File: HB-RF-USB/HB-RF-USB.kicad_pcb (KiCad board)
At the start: 2 copper layers, 47.6 x 52.1 mm, 27 parts, among them J1 USB_B_Micro, J2 Conn_02x20_Odd_Even, J3 Conn_02x06_Odd_Even, Q1 IRLML6402, Q2 IRLML6402, Q3 IRLML2502, U1 FT232RL

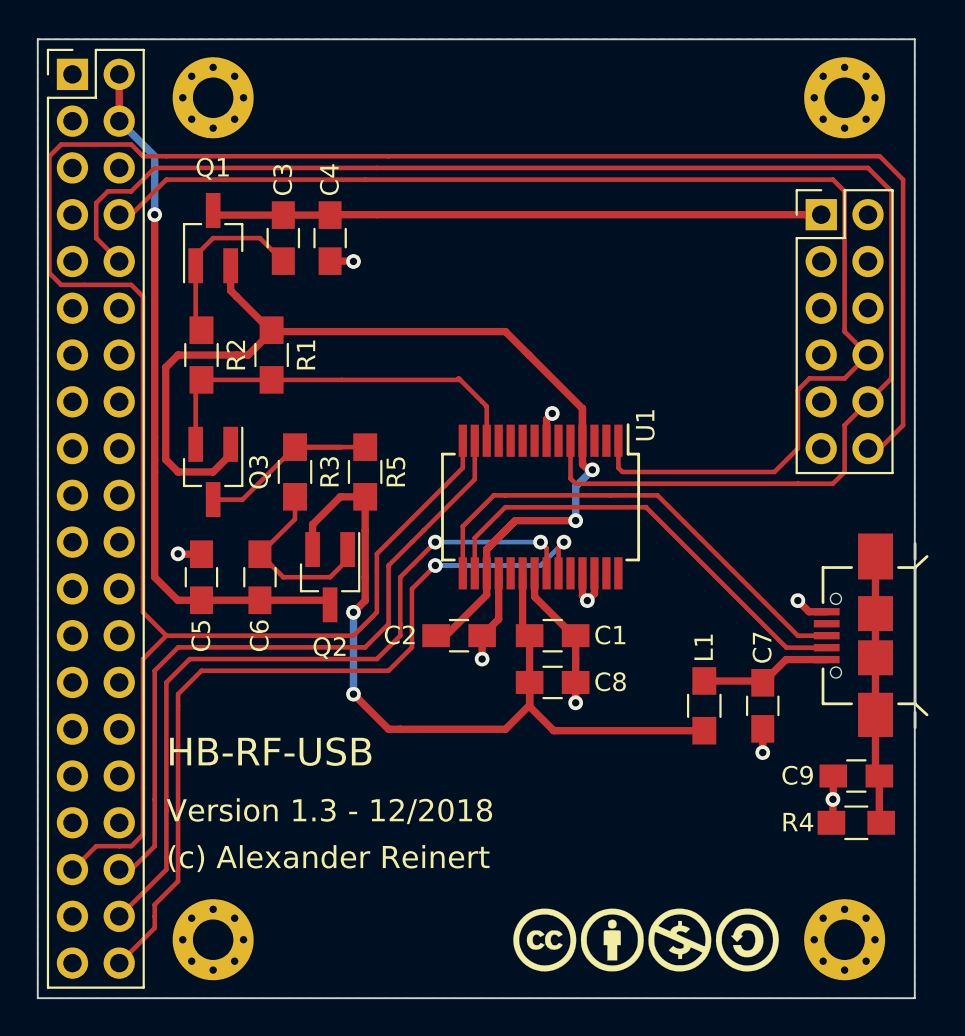
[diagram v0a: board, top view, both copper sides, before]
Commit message: - Update to Kicad 5 symbol and footprint libs
- Use different Micro USB Connector for better mechanical stability
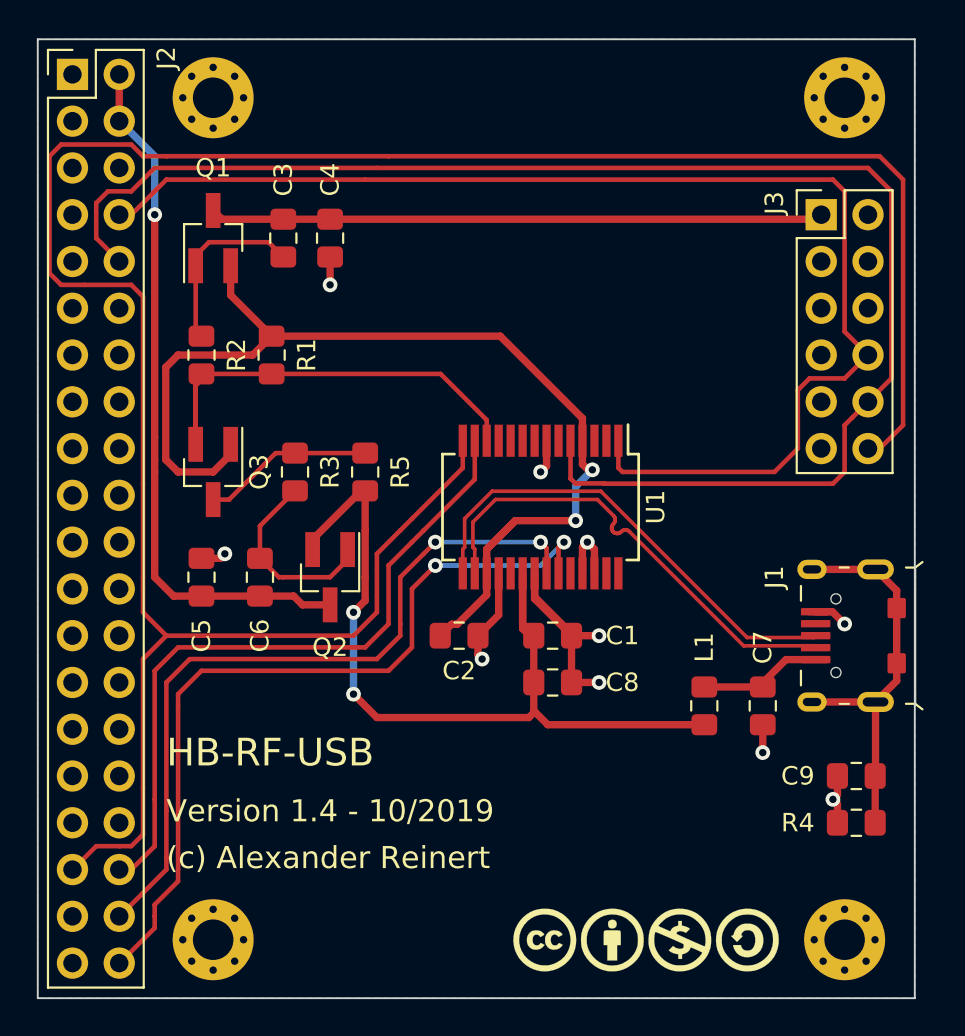
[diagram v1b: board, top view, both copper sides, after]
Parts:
- C1, C2, C3, C4, C5, C6, C7, C8, C9: footprint Capacitors_SMD:C_0805_HandSoldering -> Capacitor_SMD:C_0805_2012Metric_Pad1.15x1.40mm_HandSolder
- J1: footprint Homebrew:USB-MICRO-MK5P -> Homebrew:U-F-M5DD-Y-1
- J2: footprint Pin_Headers:Pin_Header_Straight_2x20_Pitch2.54mm -> Connector_PinHeader_2.54mm:PinHeader_2x20_P2.54mm_Vertical
- J3: footprint Pin_Headers:Pin_Header_Straight_2x06_Pitch2.54mm -> Connector_PinHeader_2.54mm:PinHeader_2x06_P2.54mm_Vertical
- L1: footprint Inductors_SMD:L_0805_HandSoldering -> Inductor_SMD:L_0805_2012Metric_Pad1.15x1.40mm_HandSolder
- Q1, Q2, Q3: footprint TO_SOT_Packages_SMD:SOT-23_Handsoldering -> Package_TO_SOT_SMD:SOT-23_Handsoldering
- R1, R2, R3, R4, R5: footprint Resistors_SMD:R_0805_HandSoldering -> Resistor_SMD:R_0805_2012Metric_Pad1.15x1.40mm_HandSolder
- U1: footprint Housings_SSOP:SSOP-28_5.3x10.2mm_Pitch0.65mm -> Package_SO:SSOP-28_5.3x10.2mm_P0.65mm
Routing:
- net GND: track 26.1 -> 34.6 mm, vias 9 -> 10
- net Net-(C9-Pad1): track 14.6 -> 22.2 mm
- net /PWREN: track 21.8 -> 25.2 mm
- net /PWREN_5V: track 12.0 -> 9.30 mm
- net +3V3: track 62.0 -> 59.9 mm
- net +5V: track 45.4 -> 46.8 mm
- net /D-: track 24.9 -> 26.0 mm
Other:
- board text added: "Version 1.4 - 10/2019"
- board text removed: "Version 1.3 - 12/2018"
